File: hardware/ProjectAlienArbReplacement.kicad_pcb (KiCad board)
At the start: 2 copper layers, 56 x 104.5 mm, 9 parts, among them J1 Bumper Connector, J3 Left Motor Connector, J4 Right Motor Connector, J5 Pixels Connector, J6 Ultrasonic Connector, J7 Micro USB, U1 4021

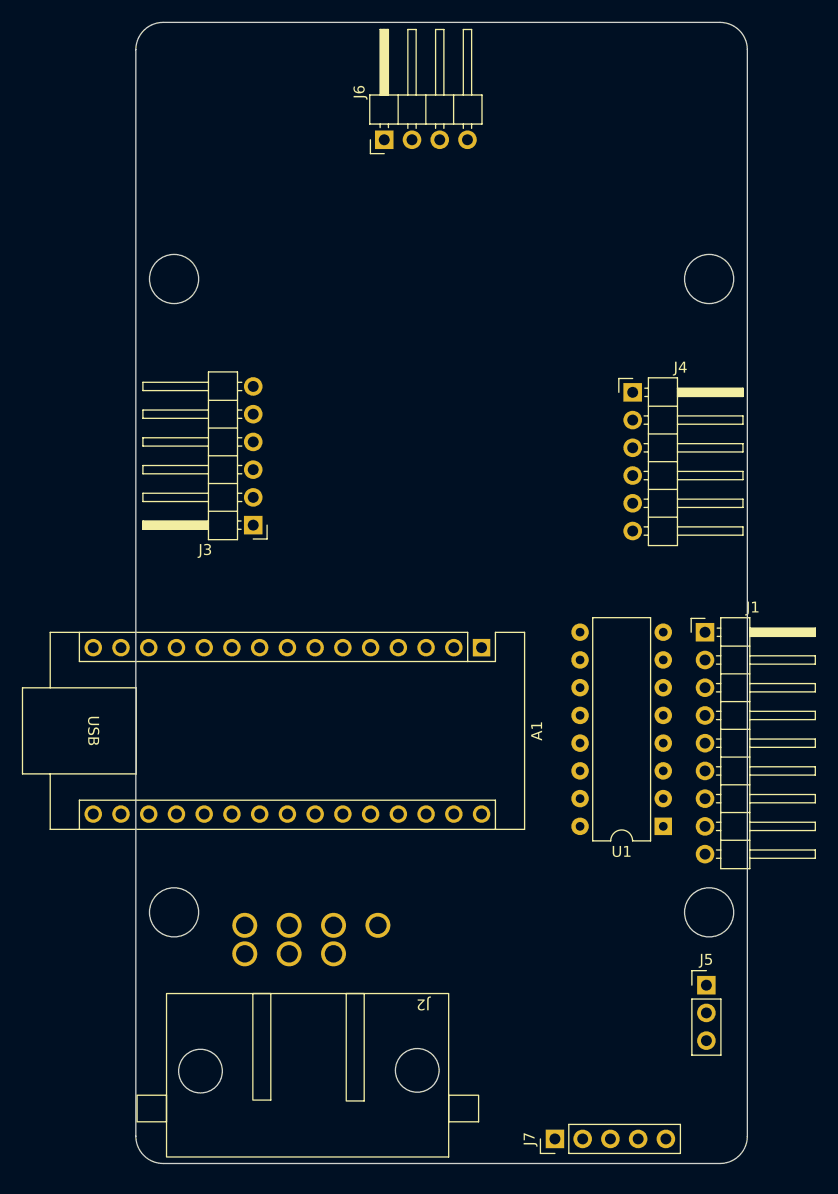
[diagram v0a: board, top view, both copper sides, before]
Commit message: Added I2C multiplexer
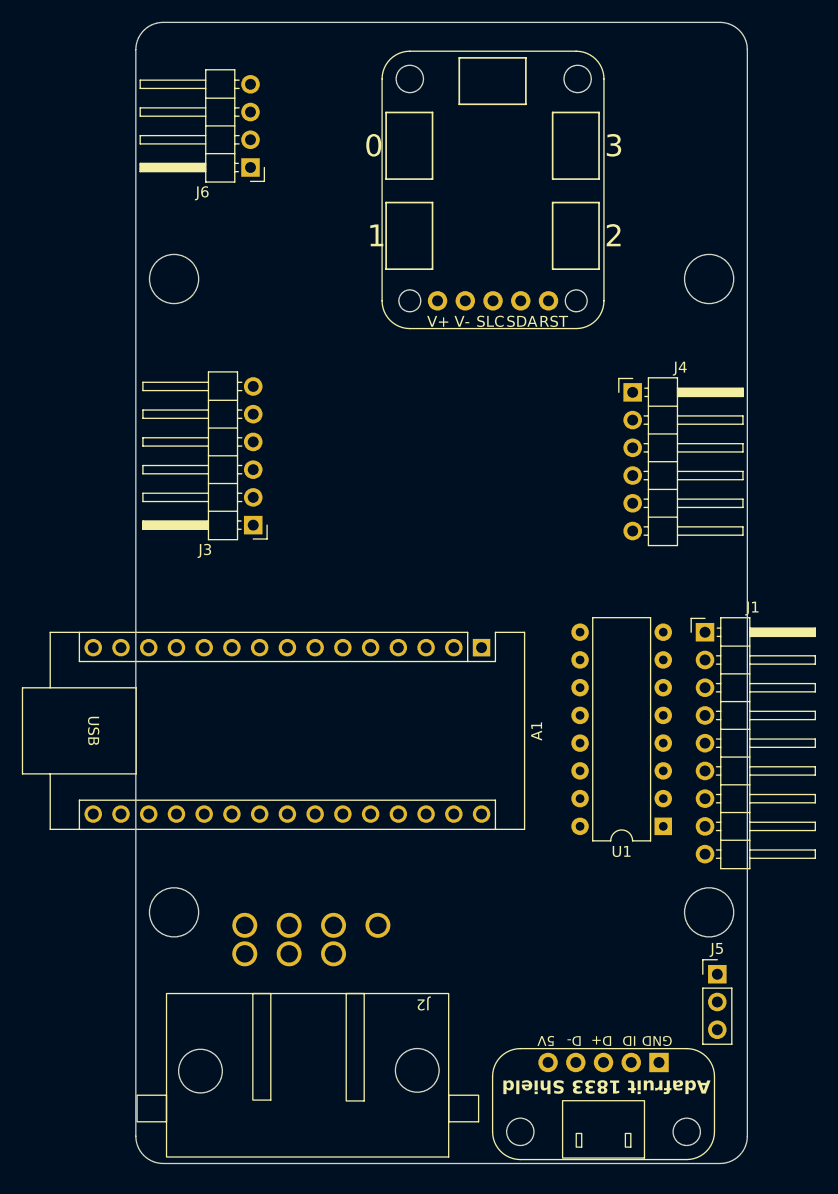
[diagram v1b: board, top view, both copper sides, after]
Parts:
- added J8: I2C Multiplexer, Adafruit_5664_Shield:Adafruit_5664_Shield, F.Cu at (143.7, 64.0)
- J7: footprint Connector_PinHeader_2.54mm:PinHeader_1x05_P2.54mm_Vertical -> Adafruit_1833_Shield:Adafruit_1833_Shield
- moved J6 12.5 mm to (121.5, 61.8), turned to 180 degrees
- moved J7 5.51 mm to (153.8, 147.5), turned to 180 degrees
- moved J5 1.41 mm to (164.2, 135.7)

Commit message: Added motor driver
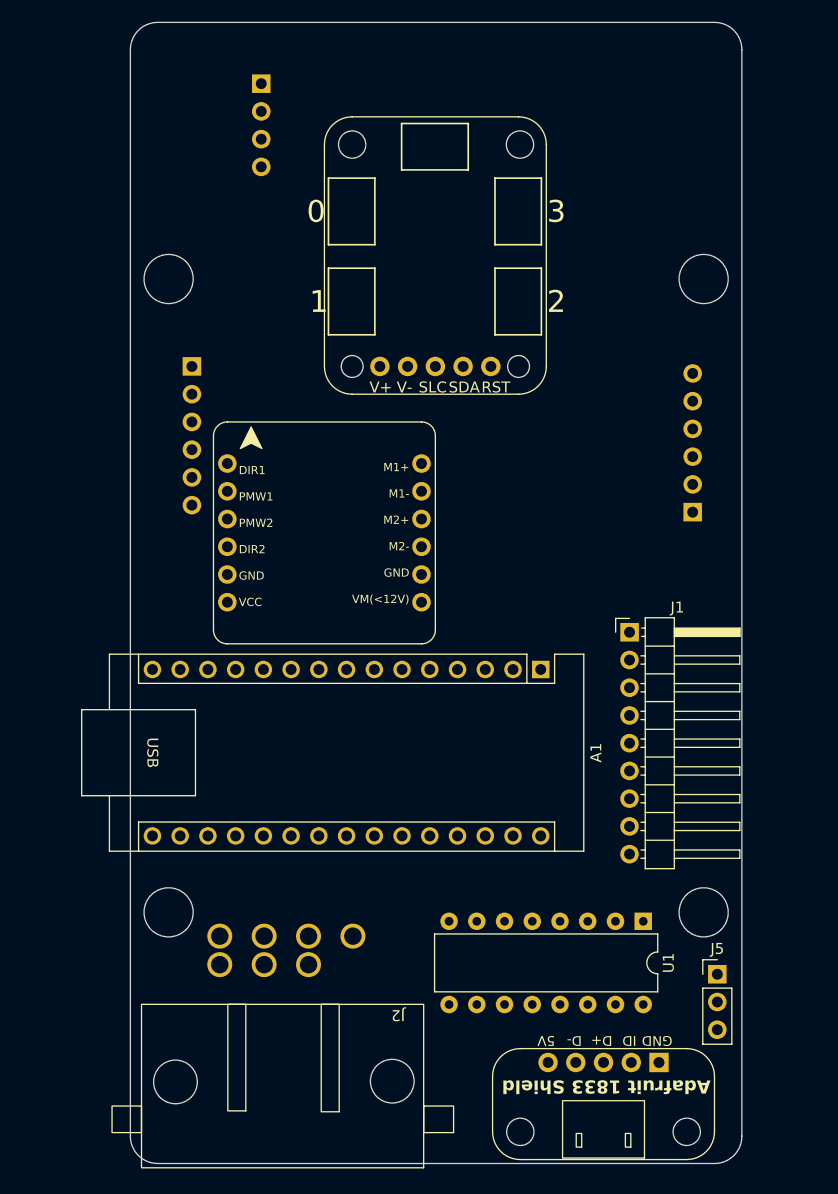
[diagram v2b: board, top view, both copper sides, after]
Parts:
- added M1: ~, DFRobot_DC_Motor_Driver_Shield:DFRobot_DC_Motor_Driver_Shield, F.Cu at (128.3, 95.3)
- J3, J4, J6: moved to B.Cu
- moved J3 15.6 mm to (116.1, 80.0)
- moved J4 12.3 mm to (162.0, 93.3)
- moved U1 8.89 mm to (157.5, 130.8), turned to -90 degrees
- moved J8 8.00 mm to (138.4, 70.0)
- moved J6 7.74 mm to (122.5, 54.1)
- moved J1 6.91 mm to (156.2, 104.3)
- moved A1 5.78 mm to (148.1, 107.8)
- moved J2 2.49 mm to (124.5, 138.4)
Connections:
- J7 pad 3: unconnected-(J7-Pin_3-Pad3) -> Net-(J7-Pin_3)

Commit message: Fixed screw hole size
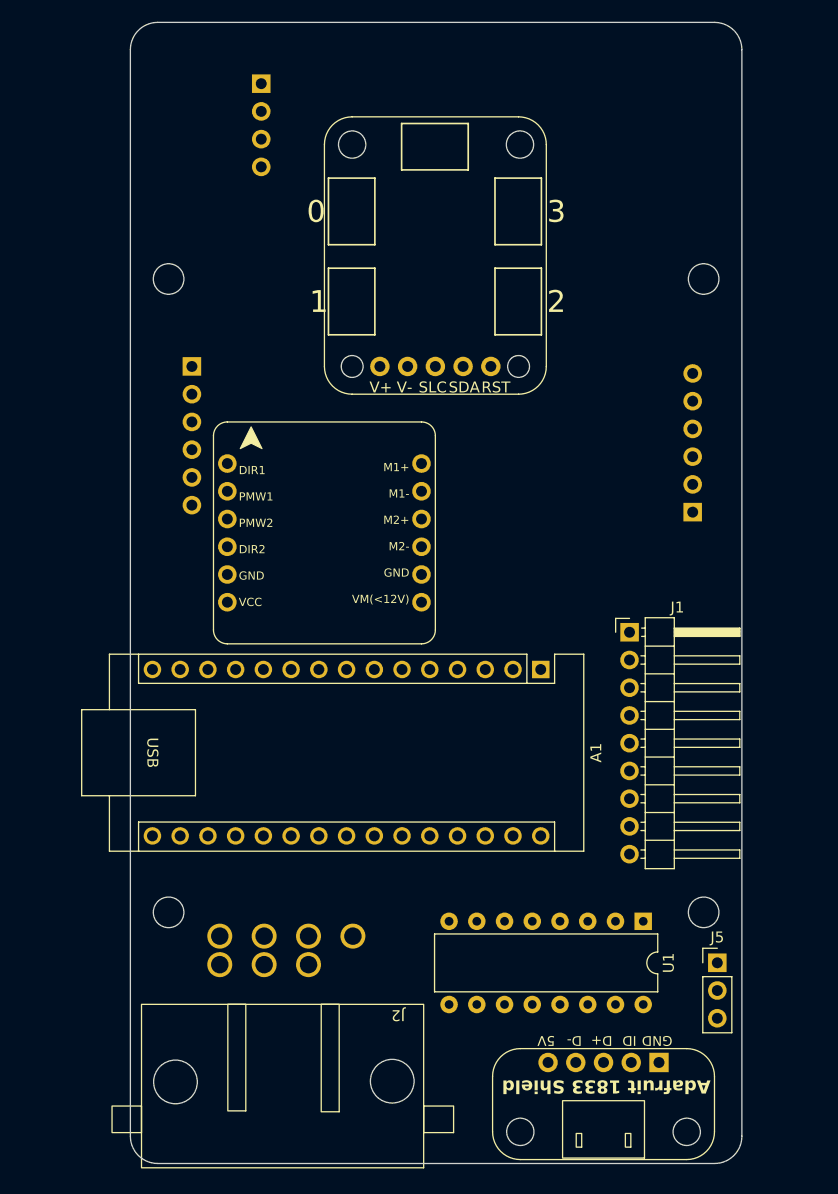
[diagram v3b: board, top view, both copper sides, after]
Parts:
- moved J5 1.05 mm to (164.2, 134.6)
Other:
- outline, holes or cut-outs redrawn
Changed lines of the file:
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@@
 	(footprint "Connector_PinHeader_2.54mm:PinHeader_1x03_P2.54mm_Vertical"
 		(layer "F.Cu")
-		(at 164.25 135.67)
+		(at 164.25 134.62)
 		(descr "Through hole straight pin header, 1x03, 2.54mm pitch, single row")
 		(tags "Through hole pin header THT 1x03 2.54mm single row")
@@
 	(gr_circle
 		(center 163 130)
-		(end 163 127.75)
+		(end 164.4 130)
 		(stroke
 			(width 0.1)
@@
 	(gr_circle
 		(center 114 72)
-		(end 114 69.75)
+		(end 115.4 72)
 		(stroke
 			(width 0.1)
@@
 	(gr_circle
 		(center 114 130)
-		(end 114 127.75)
+		(end 115.4 130)
 		(stroke
 			(width 0.1)
@@
 	(gr_circle
 		(center 163 72)
-		(end 163 69.75)
+		(end 164.4 72)
 		(stroke
 			(width 0.1)

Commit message: Updated pcb boarder
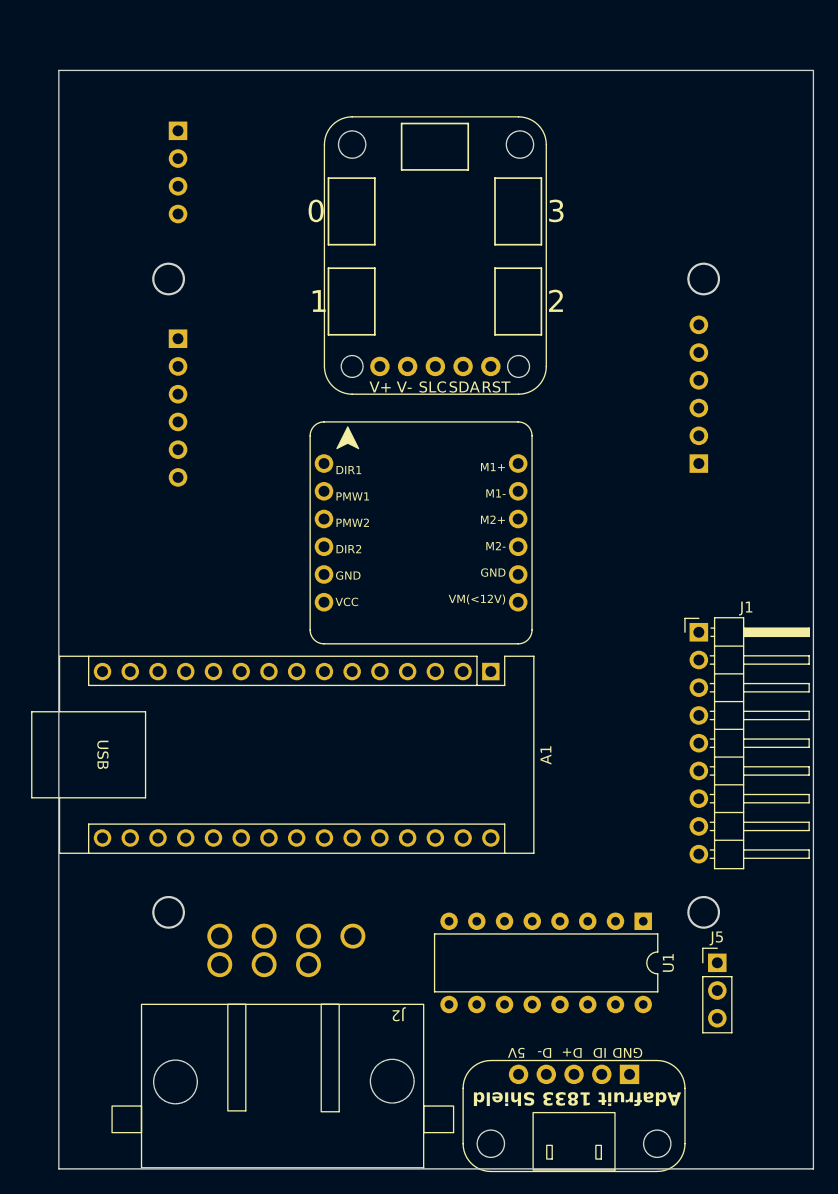
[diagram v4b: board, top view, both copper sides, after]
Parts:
- moved M1 8.85 mm to (137.2, 95.3)
- moved J6 8.76 mm to (114.9, 58.4)
- moved J1 6.35 mm to (162.6, 104.3)
- moved A1 4.57 mm to (143.5, 108.0)
- moved J4 4.49 mm to (162.6, 88.9)
- moved J7 2.91 mm to (151.1, 148.6)
- moved J3 2.84 mm to (114.9, 77.5)
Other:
- board size 56 x 104.5 mm -> 69.1 x 100.6 mm

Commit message: Plated mount holes
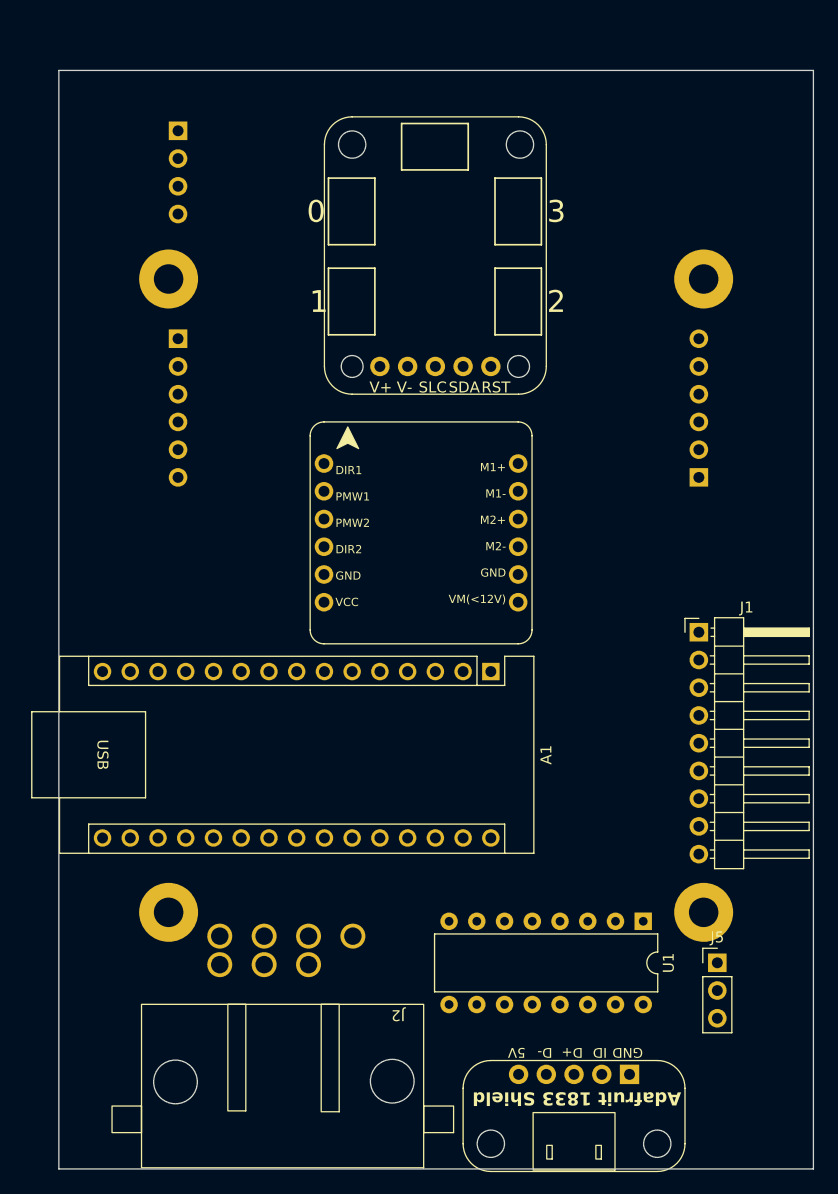
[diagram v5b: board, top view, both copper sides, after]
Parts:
- added H1: MountingHole_Pad, MountingHole:MountingHole_2.7mm_M2.5_Pad, F.Cu at (114.0, 72.0)
- added H2: MountingHole_Pad, MountingHole:MountingHole_2.7mm_M2.5_Pad, F.Cu at (114.0, 130.0)
- added H3: MountingHole_Pad, MountingHole:MountingHole_2.7mm_M2.5_Pad, F.Cu at (163.0, 130.0)
- added H4: MountingHole_Pad, MountingHole:MountingHole_2.7mm_M2.5_Pad, F.Cu at (163.0, 72.0)
- moved J4 1.27 mm to (162.6, 90.2)
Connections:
- A1 pad 12: unconnected-(A1-D9-Pad12) -> Net-(A1-D9)
- A1 pad 13: unconnected-(A1-D10-Pad13) -> Net-(A1-D10)
- A1 pad 19: unconnected-(A1-A0-Pad19) -> Net-(A1-A0)
- A1 pad 20: unconnected-(A1-A1-Pad20) -> Net-(A1-A1)
- J7 pad 3: Net-(J7-Pin_3) -> unconnected-(J7-Pin_3-Pad3)
- M1 pad 1: unconnected-(M1-DIR1-Pad1) -> Net-(A1-A0)
- M1 pad 11: Net-(J7-Pin_3) -> unconnected-(M1-M1--Pad11)
- M1 pad 2: unconnected-(M1-PMW1-Pad2) -> Net-(A1-D9)
- M1 pad 3: unconnected-(M1-PMW2-Pad3) -> Net-(A1-D10)
- M1 pad 4: unconnected-(M1-DIR2-Pad4) -> Net-(A1-A1)
- M1 pad 5: unconnected-(M1-GND-Pad5) -> GND
- M1 pad 8: unconnected-(M1-GND-Pad8) -> GND
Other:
- outline, holes or cut-outs redrawn
